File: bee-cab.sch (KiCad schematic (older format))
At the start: 40 parts, among them J1 Conn_01x02_Male, J10 Conn_01x01, J11 Conn_02x01, J12 Conn_02x01, J13 Conn_01x02, J14 Conn_01x02, J15 Conn_01x02, J16 Conn_01x02, J17 Conn_01x03, J18 Conn_01x02, J19 Conn_01x02, J2 Conn_01x02_Male, J3 Conn_01x02_Male, J4 Conn_01x02_Male, J5 Molex, J6 Conn_02x03_Odd_Even, J7 Conn_02x01, J8 Conn_01x02, J9 Conn_01x02

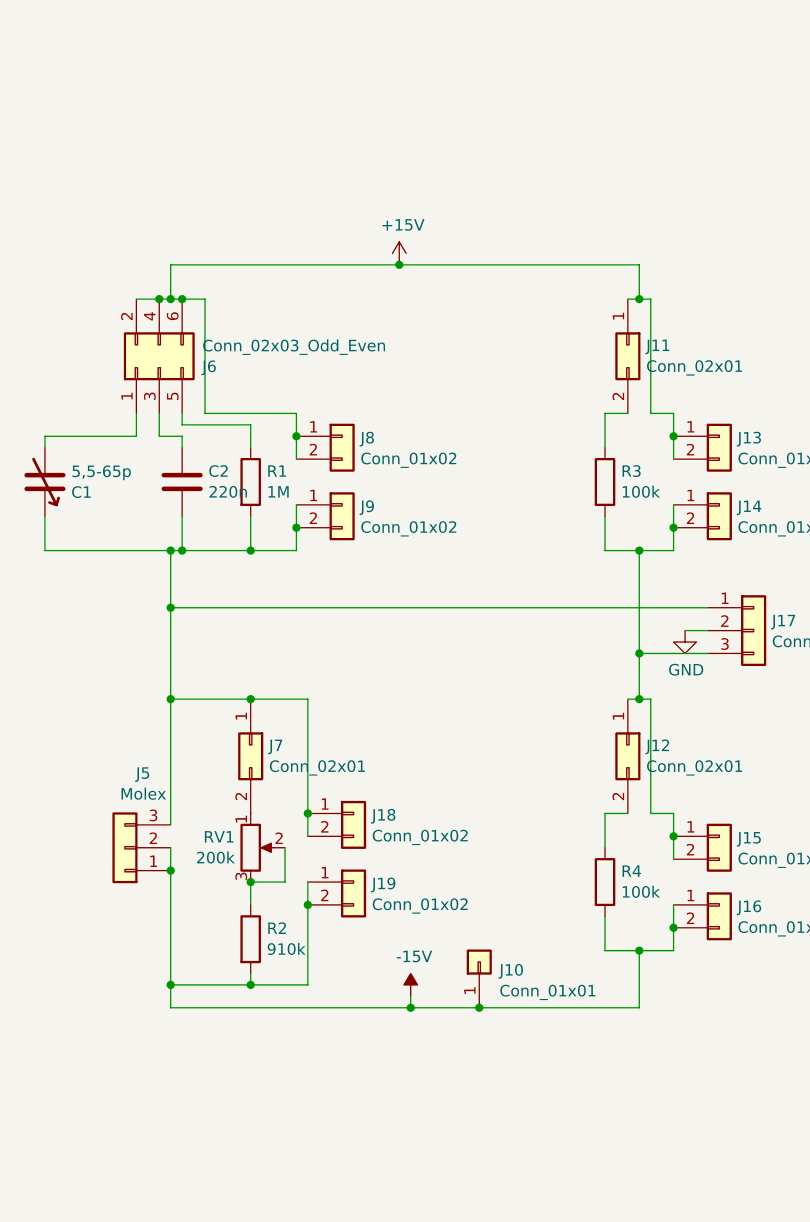
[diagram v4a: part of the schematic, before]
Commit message: Add pinheader for AC supply.
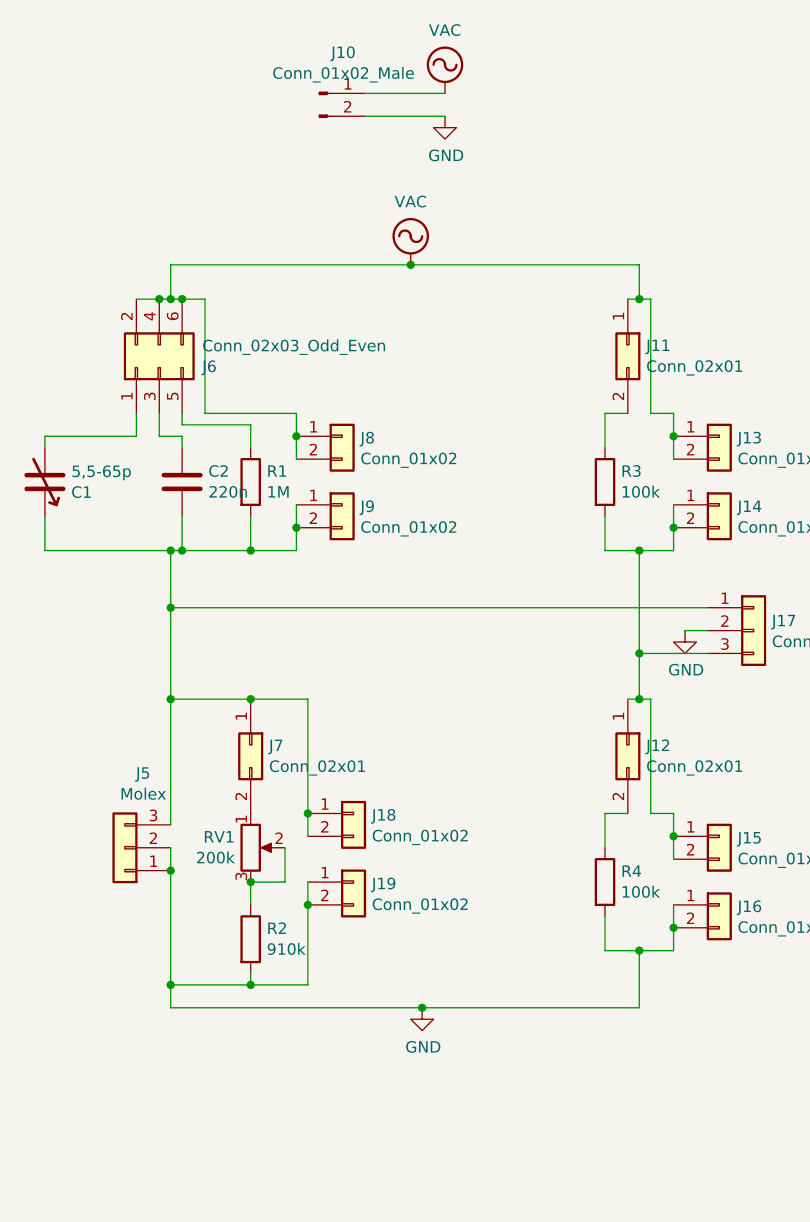
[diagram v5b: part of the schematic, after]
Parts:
- removed J10: Conn_01x01, Connector_PinHeader_2.54mm:PinHeader_1x01_P2.54mm_Vertical, symbol Connector_Generic:Conn_01x01
- added J10: Conn_01x02_Male, Connector_PinHeader_2.54mm:PinHeader_1x02_P2.54mm_Vertical, symbol Connector:Conn_01x02_Male
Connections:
- net +15V: no longer J11.1 (Pin_1), J13.1 (Pin_1), J13.2 (Pin_2), J6.2 (Pin_2), J6.4 (Pin_4), J6.6 (Pin_6), J8.1 (Pin_1), J8.2 (Pin_2)
- net -15V: no longer J16.1 (Pin_1), J16.2 (Pin_2), J19.1 (Pin_1), J19.2 (Pin_2), J5.1 (Pin_1), J5.2 (Pin_2), R2.2, R4.2
- net GND: now also J16.1 (Pin_1), J16.2 (Pin_2), J19.1 (Pin_1), J19.2 (Pin_2), J5.1 (Pin_1), J5.2 (Pin_2), R2.2, R4.2, J10.2 (Pin_2)
- new net VAC: J10.1 (Pin_1), J11.1 (Pin_1), J13.1 (Pin_1), J13.2 (Pin_2), J6.2 (Pin_2), J6.4 (Pin_4), J6.6 (Pin_6), J8.1 (Pin_1), J8.2 (Pin_2)
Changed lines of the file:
@@
 Wire Wire Line
 	3500 4600 3500 4500
-$Comp
-L power:-15V #PWR06
-U 1 1 5CC04F47
-P 4200 5000
-F 0 "#PWR06" H 4200 5100 50  0001 C CNN
-F 1 "-15V" H 4215 5173 50  0000 C CNN
-F 2 "" H 4200 5000 50  0001 C CNN
-F 3 "" H 4200 5000 50  0001 C CNN
-	1    4200 5000
-	1    0    0    -1
-$EndComp
-$Comp
-L power:+15V #PWR05
-U 1 1 5CC05E5D
-P 4150 1800
-F 0 "#PWR05" H 4150 1650 50  0001 C CNN
-F 1 "+15V" H 4165 1973 50  0000 C CNN
-F 2 "" H 4150 1800 50  0001 C CNN
-F 3 "" H 4150 1800 50  0001 C CNN
-	1    4150 1800
-	1    0    0    -1
-$EndComp
-Wire Wire Line
-	4150 1800 3150 1800
 Wire Wire Line
 	3150 1800 3150 1950
@@
 	3150 4350 3150 4450
 Wire Wire Line
-	3150 5050 4200 5050
-Wire Wire Line
-	4200 5050 4200 5000
-Wire Wire Line
 	3150 4450 3150 4950
 Connection ~ 3150 4450
 Wire Wire Line
 	3150 4250 3150 3700
-Wire Wire Line
-	4200 5050 4500 5050
-Connection ~ 4200 5050
-Connection ~ 4150 1800
-$Comp
-L Connector_Generic:Conn_01x01 J10
-U 1 1 5CC0CCD3
-P 4500 4850
-F 0 "J10" V 4464 4762 50  0000 R CNN
-F 1 "Conn_01x01" V 4373 4762 50  0000 R CNN
-F 2 "Connector_PinHeader_2.54mm:PinHeader_1x01_P2.54mm_Vertical" H 4500 4850 50  0001 C CNN
-F 3 "~" H 4500 4850 50  0001 C CNN
-F 4 "RND 205-00622" H 4500 4850 50  0001 C CNN "Reichelt Part No"
-	1    4500 4850
-	0    -1   -1   0
-$EndComp
-Connection ~ 4500 5050
 $Comp
 L Connector_Generic:Conn_01x02 J15
@@
 	5200 1950 5150 1950
 Wire Wire Line
-	4150 1800 5200 1800
-Wire Wire Line
 	5200 1950 5250 1950
 Connection ~ 5200 1950
@@
 Wire Wire Line
 	5200 4800 5200 5050
-Wire Wire Line
-	4500 5050 5200 5050
 Connection ~ 5200 4800
 Wire Wire Line
@@
 	1    0    0    -1
 $EndComp
+Wire Wire Line
+	3150 1800 4200 1800
+Wire Wire Line
+	3150 5050 4250 5050
+$Comp
+L power:VAC #PWR0105
+U 1 1 5CD565A4
+P 4350 1050
+F 0 "#PWR0105" H 4350 950 50  0001 C CNN
+F 1 "VAC" H 4350 1325 50  0000 C CNN
+F 2 "" H 4350 1050 50  0001 C CNN
+F 3 "" H 4350 1050 50  0001 C CNN
+	1    4350 1050
+	1    0    0    -1
+$EndComp
+$Comp
+L power:GND #PWR0106
+U 1 1 5CD56716
+P 4350 1150
+F 0 "#PWR0106" H 4350 900 50  0001 C CNN
+F 1 "GND" H 4355 977 50  0000 C CNN
+F 2 "" H 4350 1150 50  0001 C CNN
+F 3 "" H 4350 1150 50  0001 C CNN
+	1    4350 1150
+	1    0    0    -1
+$EndComp
+$Comp
+L Connector:Conn_01x02_Male J10
+U 1 1 5CD569BF
+P 3800 1050
+F 0 "J10" H 3906 1228 50  0000 C CNN
+F 1 "Conn_01x02_Male" H 3906 1137 50  0000 C CNN
+F 2 "Connector_PinHeader_2.54mm:PinHeader_1x02_P2.54mm_Vertical" H 3800 1050 50  0001 C CNN
+F 3 "~" H 3800 1050 50  0001 C CNN
+F 4 "RND 205-00623" H 3800 1050 50  0001 C CNN "Reichelt Part No"
+	1    3800 1050
+	1    0    0    -1
+$EndComp
+Wire Wire Line
+	4000 1050 4350 1050
+Wire Wire Line
+	4000 1150 4350 1150
+$Comp
+L power:VAC #PWR0107
+U 1 1 5CD5E157
+P 4200 1800
+F 0 "#PWR0107" H 4200 1700 50  0001 C CNN
+F 1 "VAC" H 4200 2075 50  0000 C CNN
+F 2 "" H 4200 1800 50  0001 C CNN
+F 3 "" H 4200 1800 50  0001 C CNN
+	1    4200 1800
+	1    0    0    -1
+$EndComp
+Connection ~ 4200 1800
+Wire Wire Line
+	4200 1800 5200 1800
+$Comp
+L power:GND #PWR0108
+U 1 1 5CD5E1B4
+P 4250 5050
+F 0 "#PWR0108" H 4250 4800 50  0001 C CNN
+F 1 "GND" H 4255 4877 50  0000 C CNN
+F 2 "" H 4250 5050 50  0001 C CNN
+F 3 "" H 4250 5050 50  0001 C CNN
+	1    4250 5050
+	1    0    0    -1
+$EndComp
+Connection ~ 4250 5050
+Wire Wire Line
+	4250 5050 5200 5050
 $EndSCHEMATC

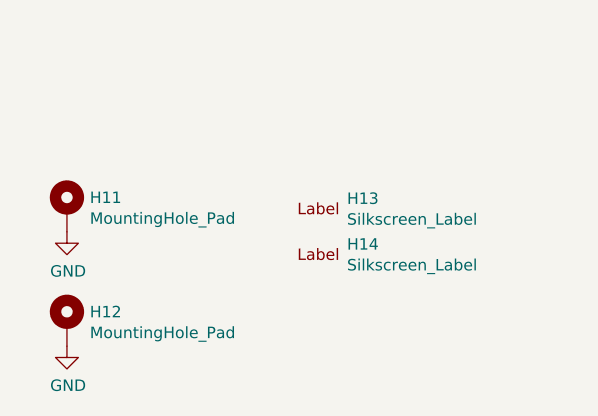
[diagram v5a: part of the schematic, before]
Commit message: Add silkscreen labels.
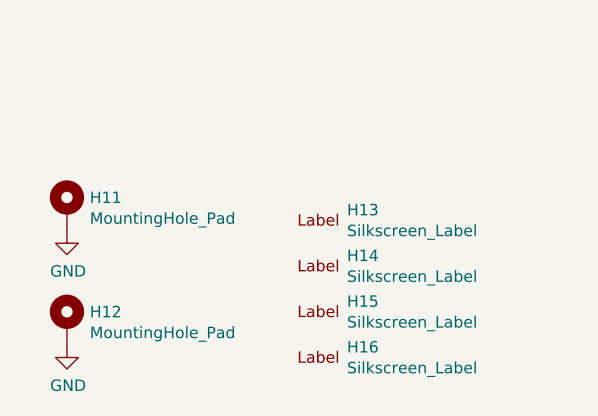
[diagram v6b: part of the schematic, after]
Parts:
- added H15: Silkscreen_Label, Symbol-emt:Text_U_S_Silkscreen, symbol Mechanical-emt:Silkscreen_Label
- added H16: Silkscreen_Label, Symbol-emt:Symbol_GND_Silkscreen, symbol Mechanical-emt:Silkscreen_Label
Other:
- moved on the sheet: H13, H14
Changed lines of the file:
@@
 L Mechanical-emt:Silkscreen_Label H13
 U 1 1 5CCCFACF
-P 5150 6900
-F 0 "H13" H 5275 6945 50  0000 L CNN
-F 1 "Silkscreen_Label" H 5275 6854 50  0000 L CNN
-F 2 "Symbol-emt:EMT-Logo_5.1x2.5mm_Silkscreen" H 5150 6900 50  0001 C CNN
-F 3 "~" H 5150 6900 50  0001 C CNN
-	1    5150 6900
+P 5150 6950
+F 0 "H13" H 5275 6995 50  0000 L CNN
+F 1 "Silkscreen_Label" H 5275 6904 50  0000 L CNN
+F 2 "Symbol-emt:EMT-Logo_5.1x2.5mm_Silkscreen" H 5150 6950 50  0001 C CNN
+F 3 "~" H 5150 6950 50  0001 C CNN
+	1    5150 6950
 	1    0    0    -1
 $EndComp
@@
 L Mechanical-emt:Silkscreen_Label H14
 U 1 1 5CCCFB83
-P 5150 7100
-F 0 "H14" H 5275 7145 50  0000 L CNN
-F 1 "Silkscreen_Label" H 5275 7054 50  0000 L CNN
-F 2 "Symbol-emt:BEE-Logo_Silkscreen_small" H 5150 7100 50  0001 C CNN
-F 3 "~" H 5150 7100 50  0001 C CNN
-	1    5150 7100
+P 5150 7150
+F 0 "H14" H 5275 7195 50  0000 L CNN
+F 1 "Silkscreen_Label" H 5275 7104 50  0000 L CNN
+F 2 "Symbol-emt:BEE-Logo_Silkscreen_small" H 5150 7150 50  0001 C CNN
+F 3 "~" H 5150 7150 50  0001 C CNN
+	1    5150 7150
 	1    0    0    -1
 $EndComp
@@
 Wire Wire Line
 	4250 5050 5200 5050
+$Comp
+L Mechanical-emt:Silkscreen_Label H15
+U 1 1 5CD6423E
+P 5150 7350
+F 0 "H15" H 5275 7395 50  0000 L CNN
+F 1 "Silkscreen_Label" H 5275 7304 50  0000 L CNN
+F 2 "Symbol-emt:Text_U_S_Silkscreen" H 5150 7350 50  0001 C CNN
+F 3 "~" H 5150 7350 50  0001 C CNN
+	1    5150 7350
+	1    0    0    -1
+$EndComp
+$Comp
+L Mechanical-emt:Silkscreen_Label H16
+U 1 1 5CD64244
+P 5150 7550
+F 0 "H16" H 5275 7595 50  0000 L CNN
+F 1 "Silkscreen_Label" H 5275 7504 50  0000 L CNN
+F 2 "Symbol-emt:Symbol_GND_Silkscreen" H 5150 7550 50  0001 C CNN
+F 3 "~" H 5150 7550 50  0001 C CNN
+	1    5150 7550
+	1    0    0    -1
+$EndComp
 $EndSCHEMATC

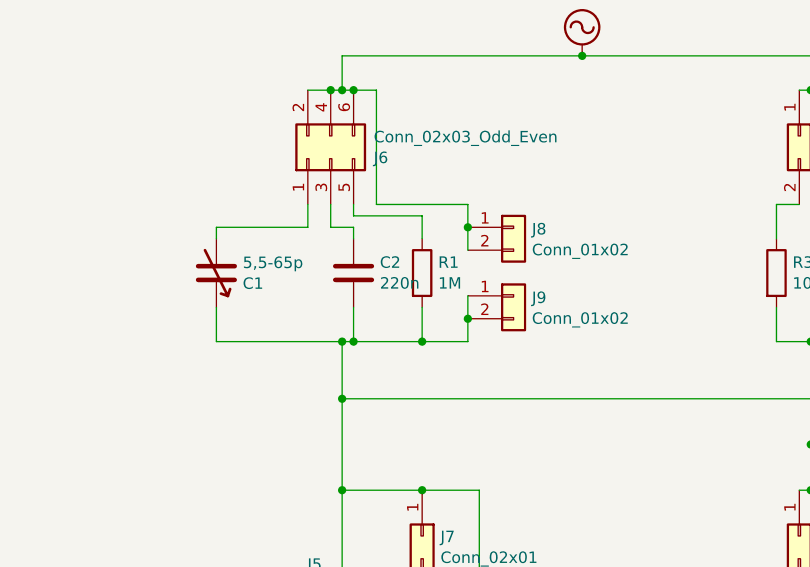
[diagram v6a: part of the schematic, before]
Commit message: Fix capacitor value.
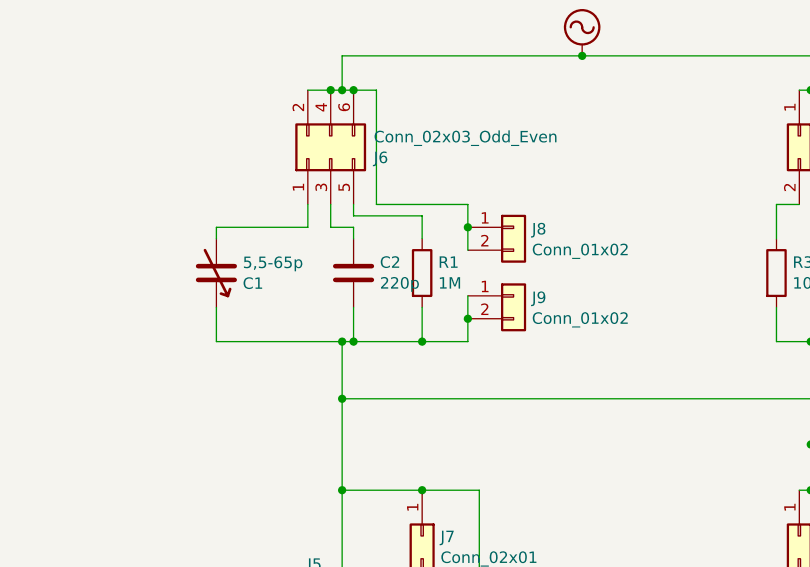
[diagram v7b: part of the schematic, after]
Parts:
- C2: value 220n -> 220p; Reichelt Part No X7R 0805 CF 220N -> NPO 0805 BJ 220P
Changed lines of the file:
@@
 P 3200 2750
 F 0 "C2" H 3315 2796 50  0000 L CNN
-F 1 "220n" H 3315 2705 50  0000 L CNN
+F 1 "220p" H 3315 2705 50  0000 L CNN
 F 2 "Capacitor_SMD:C_0805_2012Metric_Pad1.15x1.40mm_HandSolder" H 3238 2600 50  0001 C CNN
 F 3 "~" H 3200 2750 50  0001 C CNN
-F 4 "X7R 0805 CF 220N" H 3200 2750 50  0001 C CNN "Reichelt Part No"
+F 4 "NPO 0805 BJ 220P" H 3200 2750 50  0001 C CNN "Reichelt Part No"
 	1    3200 2750
 	1    0    0    -1

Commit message: Relabel as bee specific.
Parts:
- C1: footprint Capacitor_THT-emt:C_Trimmer_Vishay_D10mm_Vertical_HolePattern5mmx10mm -> Capacitor_THT-bee:C_Trimmer_Vishay_D10mm_Vertical_HolePattern5mmx10mm
- H1, H2: footprint Symbol-emt:Text_U_B+_Silkscreen -> Symbol-bee:Text_U_B+_Silkscreen; symbol Mechanical-emt:Silkscreen_Label -> Mechanical-bee:Silkscreen_Label
- H13: footprint Symbol-emt:EMT-Logo_5.1x2.5mm_Silkscreen -> Symbol-bee:EMT-Logo_5.1x2.5mm_Silkscreen; symbol Mechanical-emt:Silkscreen_Label -> Mechanical-bee:Silkscreen_Label
- H14: footprint Symbol-emt:BEE-Logo_Silkscreen_small -> Symbol-bee:BEE-Logo_Silkscreen_small; symbol Mechanical-emt:Silkscreen_Label -> Mechanical-bee:Silkscreen_Label
- H15: footprint Symbol-emt:Text_U_S_Silkscreen -> Symbol-bee:Text_U_S_Silkscreen; symbol Mechanical-emt:Silkscreen_Label -> Mechanical-bee:Silkscreen_Label
- H16, H7, H8: footprint Symbol-emt:Symbol_GND_Silkscreen -> Symbol-bee:Symbol_GND_Silkscreen; symbol Mechanical-emt:Silkscreen_Label -> Mechanical-bee:Silkscreen_Label
- H3, H4: footprint Symbol-emt:Text_U_B-_Silkscreen -> Symbol-bee:Text_U_B-_Silkscreen; symbol Mechanical-emt:Silkscreen_Label -> Mechanical-bee:Silkscreen_Label
- H5, H6: footprint Symbol-emt:Text_U_B2_Silkscreen -> Symbol-bee:Text_U_B2_Silkscreen; symbol Mechanical-emt:Silkscreen_Label -> Mechanical-bee:Silkscreen_Label
- J5: footprint Connector_Molex-emt:Molex_Easy-On_528070310_1x03_P1.0mm_Horizontal -> Connector_Molex-bee:Molex_Easy-On_528070310_1x03_P1.0mm_Horizontal
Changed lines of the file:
@@
 F 0 "C1" H 2715 2796 50  0000 L CNN
 F 1 "5,5-65p" H 2715 2705 50  0000 L CNN
-F 2 "Capacitor_THT-emt:C_Trimmer_Vishay_D10mm_Vertical_HolePattern5mmx10mm" H 2600 2750 50  0001 C CNN
+F 2 "Capacitor_THT-bee:C_Trimmer_Vishay_D10mm_Vertical_HolePattern5mmx10mm" H 2600 2750 50  0001 C CNN
 F 3 "~" H 2600 2750 50  0001 C CNN
 F 4 "TRIMMER 31659" H 2600 2750 50  0001 C CNN "Reichelt Part No"
@@
 F 0 "J5" H 2870 4025 50  0000 C CNN
 F 1 "Molex" H 2870 4116 50  0000 C CNN
-F 2 "Connector_Molex-emt:Molex_Easy-On_528070310_1x03_P1.0mm_Horizontal" H 2950 4350 50  0001 C CNN
+F 2 "Connector_Molex-bee:Molex_Easy-On_528070310_1x03_P1.0mm_Horizontal" H 2950 4350 50  0001 C CNN
 F 3 "~" H 2950 4350 50  0001 C CNN
 F 4 "538-52807-0310" H 2950 4350 50  0001 C CNN "Mouser Part No"
@@
 	2600 2900 2600 3050
 $Comp
-L Mechanical-emt:Silkscreen_Label H4
+L Mechanical-bee:Silkscreen_Label H4
 U 1 1 5CC7DACB
 P 800 7550
 F 0 "H4" H 925 7595 50  0000 L CNN
 F 1 "Silkscreen_Label" H 925 7504 50  0000 L CNN
-F 2 "Symbol-emt:Text_U_B-_Silkscreen" H 800 7550 50  0001 C CNN
+F 2 "Symbol-bee:Text_U_B-_Silkscreen" H 800 7550 50  0001 C CNN
 F 3 "~" H 800 7550 50  0001 C CNN
 	1    800  7550
@@
 $EndComp
 $Comp
-L Mechanical-emt:Silkscreen_Label H3
+L Mechanical-bee:Silkscreen_Label H3
 U 1 1 5CC7E4B0
 P 800 7350
 F 0 "H3" H 925 7395 50  0000 L CNN
 F 1 "Silkscreen_Label" H 925 7304 50  0000 L CNN
-F 2 "Symbol-emt:Text_U_B-_Silkscreen" H 800 7350 50  0001 C CNN
+F 2 "Symbol-bee:Text_U_B-_Silkscreen" H 800 7350 50  0001 C CNN
 F 3 "~" H 800 7350 50  0001 C CNN
 	1    800  7350
@@
 $EndComp
 $Comp
-L Mechanical-emt:Silkscreen_Label H2
+L Mechanical-bee:Silkscreen_Label H2
 U 1 1 5CC7E7BF
 P 800 7150
 F 0 "H2" H 925 7195 50  0000 L CNN
 F 1 "Silkscreen_Label" H 925 7104 50  0000 L CNN
-F 2 "Symbol-emt:Text_U_B+_Silkscreen" H 800 7150 50  0001 C CNN
+F 2 "Symbol-bee:Text_U_B+_Silkscreen" H 800 7150 50  0001 C CNN
 F 3 "~" H 800 7150 50  0001 C CNN
 	1    800  7150
@@
 $EndComp
 $Comp
-L Mechanical-emt:Silkscreen_Label H1
+L Mechanical-bee:Silkscreen_Label H1
 U 1 1 5CC7EB64
 P 800 6950
 F 0 "H1" H 925 6995 50  0000 L CNN
 F 1 "Silkscreen_Label" H 925 6904 50  0000 L CNN
-F 2 "Symbol-emt:Text_U_B+_Silkscreen" H 800 6950 50  0001 C CNN
+F 2 "Symbol-bee:Text_U_B+_Silkscreen" H 800 6950 50  0001 C CNN
 F 3 "~" H 800 6950 50  0001 C CNN
 	1    800  6950
@@
 $EndComp
 $Comp
-L Mechanical-emt:Silkscreen_Label H5
+L Mechanical-bee:Silkscreen_Label H5
 U 1 1 5CC7EED7
 P 1700 6950
 F 0 "H5" H 1825 6995 50  0000 L CNN
 F 1 "Silkscreen_Label" H 1825 6904 50  0000 L CNN
-F 2 "Symbol-emt:Text_U_B2_Silkscreen" H 1700 6950 50  0001 C CNN
+F 2 "Symbol-bee:Text_U_B2_Silkscreen" H 1700 6950 50  0001 C CNN
 F 3 "~" H 1700 6950 50  0001 C CNN
 	1    1700 6950
@@
 $EndComp
 $Comp
-L Mechanical-emt:Silkscreen_Label H6
+L Mechanical-bee:Silkscreen_Label H6
 U 1 1 5CC7F429
 P 1700 7150
 F 0 "H6" H 1825 7195 50  0000 L CNN
 F 1 "Silkscreen_Label" H 1825 7104 50  0000 L CNN
-F 2 "Symbol-emt:Text_U_B2_Silkscreen" H 1700 7150 50  0001 C CNN
+F 2 "Symbol-bee:Text_U_B2_Silkscreen" H 1700 7150 50  0001 C CNN
 F 3 "~" H 1700 7150 50  0001 C CNN
 	1    1700 7150
@@
 $EndComp
 $Comp
-L Mechanical-emt:Silkscreen_Label H7
+L Mechanical-bee:Silkscreen_Label H7
 U 1 1 5CC7F75B
 P 1700 7350
 F 0 "H7" H 1825 7395 50  0000 L CNN
 F 1 "Silkscreen_Label" H 1825 7304 50  0000 L CNN
-F 2 "Symbol-emt:Symbol_GND_Silkscreen" H 1700 7350 50  0001 C CNN
+F 2 "Symbol-bee:Symbol_GND_Silkscreen" H 1700 7350 50  0001 C CNN
 F 3 "~" H 1700 7350 50  0001 C CNN
 	1    1700 7350
@@
 $EndComp
 $Comp
-L Mechanical-emt:Silkscreen_Label H8
+L Mechanical-bee:Silkscreen_Label H8
 U 1 1 5CC7FA9C
 P 1700 7550
 F 0 "H8" H 1825 7595 50  0000 L CNN
 F 1 "Silkscreen_Label" H 1825 7504 50  0000 L CNN
-F 2 "Symbol-emt:Symbol_GND_Silkscreen" H 1700 7550 50  0001 C CNN
+F 2 "Symbol-bee:Symbol_GND_Silkscreen" H 1700 7550 50  0001 C CNN
 F 3 "~" H 1700 7550 50  0001 C CNN
 	1    1700 7550
@@
 $EndComp
 $Comp
-L Mechanical-emt:Silkscreen_Label H13
+L Mechanical-bee:Silkscreen_Label H13
 U 1 1 5CCCFACF
 P 5150 6950
 F 0 "H13" H 5275 6995 50  0000 L CNN
 F 1 "Silkscreen_Label" H 5275 6904 50  0000 L CNN
-F 2 "Symbol-emt:EMT-Logo_5.1x2.5mm_Silkscreen" H 5150 6950 50  0001 C CNN
+F 2 "Symbol-bee:EMT-Logo_5.1x2.5mm_Silkscreen" H 5150 6950 50  0001 C CNN
 F 3 "~" H 5150 6950 50  0001 C CNN
 	1    5150 6950
@@
 $EndComp
 $Comp
-L Mechanical-emt:Silkscreen_Label H14
+L Mechanical-bee:Silkscreen_Label H14
 U 1 1 5CCCFB83
 P 5150 7150
 F 0 "H14" H 5275 7195 50  0000 L CNN
 F 1 "Silkscreen_Label" H 5275 7104 50  0000 L CNN
-F 2 "Symbol-emt:BEE-Logo_Silkscreen_small" H 5150 7150 50  0001 C CNN
+F 2 "Symbol-bee:BEE-Logo_Silkscreen_small" H 5150 7150 50  0001 C CNN
 F 3 "~" H 5150 7150 50  0001 C CNN
 	1    5150 7150
@@
 	4250 5050 5200 5050
 $Comp
-L Mechanical-emt:Silkscreen_Label H15
+L Mechanical-bee:Silkscreen_Label H15
 U 1 1 5CD6423E
 P 5150 7350
 F 0 "H15" H 5275 7395 50  0000 L CNN
 F 1 "Silkscreen_Label" H 5275 7304 50  0000 L CNN
-F 2 "Symbol-emt:Text_U_S_Silkscreen" H 5150 7350 50  0001 C CNN
+F 2 "Symbol-bee:Text_U_S_Silkscreen" H 5150 7350 50  0001 C CNN
 F 3 "~" H 5150 7350 50  0001 C CNN
 	1    5150 7350
@@
 $EndComp
 $Comp
-L Mechanical-emt:Silkscreen_Label H16
+L Mechanical-bee:Silkscreen_Label H16
 U 1 1 5CD64244
 P 5150 7550
 F 0 "H16" H 5275 7595 50  0000 L CNN
 F 1 "Silkscreen_Label" H 5275 7504 50  0000 L CNN
-F 2 "Symbol-emt:Symbol_GND_Silkscreen" H 5150 7550 50  0001 C CNN
+F 2 "Symbol-bee:Symbol_GND_Silkscreen" H 5150 7550 50  0001 C CNN
 F 3 "~" H 5150 7550 50  0001 C CNN
 	1    5150 7550
